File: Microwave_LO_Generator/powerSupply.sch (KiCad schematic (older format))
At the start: 33 parts, among them J1 Conn_01x02_Male, J2 Conn_01x02_Male, U2 LT1962-3.3, U3 LT3010, U5 LT1962-5, U6 LT1962-5

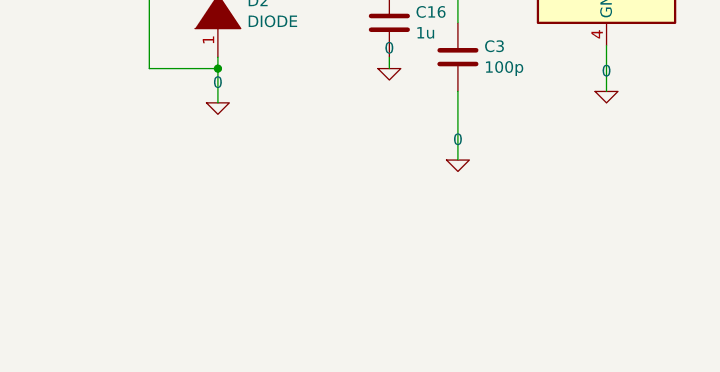
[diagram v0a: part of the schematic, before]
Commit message: ADD GND test probe
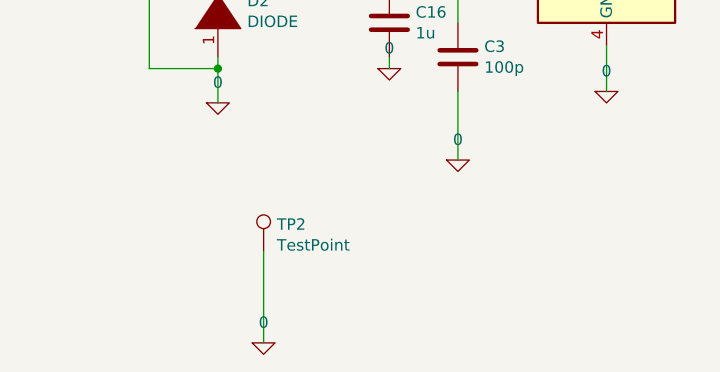
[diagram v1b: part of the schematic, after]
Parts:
- added TP2: TestPoint, TestPoint:TestPoint_Loop_D2.60mm_Drill1.6mm_Beaded, symbol frequencySynthesizer-rescue:TestPoint-frequencySintesizer
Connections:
- net 0: now also TP2.1
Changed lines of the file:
@@
 Wire Wire Line
 	6300 2050 6300 2300
+$Comp
+L pspice:0 #GND0136
+U 1 1 5FCEC166
+P 1750 5400
+F 0 "#GND0136" H 1750 5300 50  0001 C CNN
+F 1 "0" H 1750 5489 50  0000 C CNN
+F 2 "" H 1750 5400 50  0001 C CNN
+F 3 "~" H 1750 5400 50  0001 C CNN
+	1    1750 5400
+	1    0    0    -1
+$EndComp
+$Comp
+L frequencySynthesizer-rescue:TestPoint-frequencySintesizer TP?
+U 1 1 5FCF081C
+P 1750 5000
+AR Path="/5FBD30A7/5FCF081C" Ref="TP?"  Part="1"
+AR Path="/5FBD5B32/5FCF081C" Ref="TP2"  Part="1"
+F 0 "TP2" H 1808 5118 50  0000 L CNN
+F 1 "TestPoint" H 1808 5027 50  0000 L CNN
+F 2 "TestPoint:TestPoint_Loop_D2.60mm_Drill1.6mm_Beaded" H 1950 5000 50  0001 C CNN
+F 3 "https://www.mouser.it/datasheet/2/215/005-5009-741293.pdf" H 1950 5000 50  0001 C CNN
+F 4 "5007" H 1750 5000 50  0001 C CNN "Manufacturer/Part Number"
+F 5 "Mouser 534-5007" H 1750 5000 50  0001 C CNN "Supplier Stock Code"
+	1    1750 5000
+	1    0    0    -1
+$EndComp
+Wire Wire Line
+	1750 5000 1750 5400
 $EndSCHEMATC

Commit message: backup
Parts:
- C16: Manufacturer/Part Number GCM1555C1H101JA16D -> 963-GMK105CC6105MV-F; Supplier Stock Code Mouser 81-GCM1555C1H101JA6D -> GMK105CC6105MV-F
- C17, C19, C23: Manufacturer/Part Number GCM1555C1H101JA16D -> 0402YD475MAT2A; Supplier Stock Code Mouser 81-GCM1555C1H101JA6D -> 581-0402YD475MAT2A
- C21, C24, C31: Supplier Stock Code Mouser 81-GCM1555C1H101JA6D -> 81-GCM1555C1H101JA6D
- C22: Manufacturer/Part Number GCM1555C1H101JA16D -> GMK105CC6105MV-F; Supplier Stock Code Mouser 81-GCM1555C1H101JA6D -> 963-GMK105CC6105MV-F
- C25, C35, C36: Manufacturer/Part Number GCM1555C1H101JA16D -> C1005X5R1A335K050BC; Supplier Stock Code Mouser 81-GCM1555C1H101JA6D -> 810-C1005X5R1A335K0C
- C3, C5: Manufacturer/Part Number GCM1555C1H101JA16D -> 04025C101KAT2A; Supplier Stock Code Mouser 81-GCM1555C1H101JA6D -> 581-04025C101KAT2A
- C32, C33, C34: Manufacturer/Part Number GCM1555C1H101JA16D -> 0402YC103KAT4A; Supplier Stock Code Mouser 81-GCM1555C1H101JA6D -> 581-0402YC103KAT4A
- D2, D3: Manufacturer/Part Number (none) -> LL4002G; Supplier Stock Code (none) -> 821-LL4002G
- D7: Manufacturer/Part Number HSMG-C170 -> AP2012HD; Supplier Stock Code Mouser 630-HSMG-C170 -> 604-AP2012HD
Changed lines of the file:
@@
 F 2 "Capacitor_SMD:C_0402_1005Metric_Pad0.74x0.62mm_HandSolder" H 2338 3850 50  0001 C CNN
 F 3 "~" H 2300 4000 50  0001 C CNN
-F 4 "GCM1555C1H101JA16D" H 2300 4000 50  0001 C CNN "Manufacturer/Part Number"
-F 5 "Mouser 81-GCM1555C1H101JA6D" H 2300 4000 50  0001 C CNN "Supplier Stock Code"
+F 4 "963-GMK105CC6105MV-F" H 2300 4000 50  0001 C CNN "Manufacturer/Part Number"
+F 5 "GMK105CC6105MV-F" H 2300 4000 50  0001 C CNN "Supplier Stock Code"
 	1    2300 4000
 	-1   0    0    1
@@
 F 2 "Diode_SMD:D_MELF" H 1550 3950 50  0001 C CNN
 F 3 "~" H 1550 3950 50  0001 C CNN
+F 4 "LL4002G" V 1550 3950 50  0001 C CNN "Manufacturer/Part Number"
+F 5 "821-LL4002G" V 1550 3950 50  0001 C CNN "Supplier Stock Code"
 	1    1550 3950
 	0    -1   -1   0
@@
 F 2 "Capacitor_SMD:C_0402_1005Metric_Pad0.74x0.62mm_HandSolder" H 4938 3850 50  0001 C CNN
 F 3 "~" H 4900 4000 50  0001 C CNN
-F 4 "GCM1555C1H101JA16D" H 4900 4000 50  0001 C CNN "Manufacturer/Part Number"
-F 5 "Mouser 81-GCM1555C1H101JA6D" H 4900 4000 50  0001 C CNN "Supplier Stock Code"
+F 4 "GMK105CC6105MV-F" H 4900 4000 50  0001 C CNN "Manufacturer/Part Number"
+F 5 "963-GMK105CC6105MV-F" H 4900 4000 50  0001 C CNN "Supplier Stock Code"
 	1    4900 4000
 	-1   0    0    1
@@
 F 2 "Capacitor_SMD:C_0402_1005Metric_Pad0.74x0.62mm_HandSolder" H 7388 1750 50  0001 C CNN
 F 3 "~" H 7350 1900 50  0001 C CNN
-F 4 "GCM1555C1H101JA16D" H 7350 1900 50  0001 C CNN "Manufacturer/Part Number"
-F 5 "Mouser 81-GCM1555C1H101JA6D" H 7350 1900 50  0001 C CNN "Supplier Stock Code"
+F 4 "0402YD475MAT2A" H 7350 1900 50  0001 C CNN "Manufacturer/Part Number"
+F 5 "581-0402YD475MAT2A" H 7350 1900 50  0001 C CNN "Supplier Stock Code"
 	1    7350 1900
 	-1   0    0    1
@@
 F 3 "~" H 7800 2050 50  0001 C CNN
 F 4 "GCM1555C1H101JA16D" H 7800 2050 50  0001 C CNN "Manufacturer/Part Number"
-F 5 "Mouser 81-GCM1555C1H101JA6D" H 7800 2050 50  0001 C CNN "Supplier Stock Code"
+F 5 "81-GCM1555C1H101JA6D" H 7800 2050 50  0001 C CNN "Supplier Stock Code"
 	1    7800 2050
 	-1   0    0    1
@@
 F 2 "Capacitor_SMD:C_0402_1005Metric_Pad0.74x0.62mm_HandSolder" H 9838 1750 50  0001 C CNN
 F 3 "~" H 9800 1900 50  0001 C CNN
-F 4 "GCM1555C1H101JA16D" H 9800 1900 50  0001 C CNN "Manufacturer/Part Number"
-F 5 "Mouser 81-GCM1555C1H101JA6D" H 9800 1900 50  0001 C CNN "Supplier Stock Code"
+F 4 "C1005X5R1A335K050BC" H 9800 1900 50  0001 C CNN "Manufacturer/Part Number"
+F 5 "810-C1005X5R1A335K0C" H 9800 1900 50  0001 C CNN "Supplier Stock Code"
 	1    9800 1900
 	-1   0    0    1
@@
 F 2 "LED_SMD:LED_0805_2012Metric_Pad1.15x1.40mm_HandSolder" H 10250 2300 50  0001 C CNN
 F 3 "https://www.mouser.it/datasheet/2/678/av02-0551en-ds-hsmx-cxxx-05mar2012-1827675.pdf" H 10250 2300 50  0001 C CNN
-F 4 "HSMG-C170" H 10250 2300 50  0001 C CNN "Manufacturer/Part Number"
-F 5 "Mouser 630-HSMG-C170" H 10250 2300 50  0001 C CNN "Supplier Stock Code"
+F 4 "AP2012HD" H 10250 2300 50  0001 C CNN "Manufacturer/Part Number"
+F 5 "604-AP2012HD" H 10250 2300 50  0001 C CNN "Supplier Stock Code"
 	1    10250 2300
 	0    -1   -1   0
@@
 F 2 "Capacitor_SMD:C_0402_1005Metric_Pad0.74x0.62mm_HandSolder" H 9938 3350 50  0001 C CNN
 F 3 "~" H 9900 3500 50  0001 C CNN
-F 4 "GCM1555C1H101JA16D" H 9900 3500 50  0001 C CNN "Manufacturer/Part Number"
-F 5 "Mouser 81-GCM1555C1H101JA6D" H 9900 3500 50  0001 C CNN "Supplier Stock Code"
+F 4 "C1005X5R1A335K050BC" H 9900 3500 50  0001 C CNN "Manufacturer/Part Number"
+F 5 "810-C1005X5R1A335K0C" H 9900 3500 50  0001 C CNN "Supplier Stock Code"
 	1    9900 3500
 	-1   0    0    1
@@
 F 2 "Capacitor_SMD:C_0402_1005Metric_Pad0.74x0.62mm_HandSolder" H 9438 3300 50  0001 C CNN
 F 3 "~" H 9400 3450 50  0001 C CNN
-F 4 "GCM1555C1H101JA16D" H 9400 3450 50  0001 C CNN "Manufacturer/Part Number"
-F 5 "Mouser 81-GCM1555C1H101JA6D" H 9400 3450 50  0001 C CNN "Supplier Stock Code"
+F 4 "0402YC103KAT4A" H 9400 3450 50  0001 C CNN "Manufacturer/Part Number"
+F 5 "581-0402YC103KAT4A" H 9400 3450 50  0001 C CNN "Supplier Stock Code"
 	1    9400 3450
 	-1   0    0    1
@@
 F 2 "Capacitor_SMD:C_0402_1005Metric_Pad0.74x0.62mm_HandSolder" H 9338 1700 50  0001 C CNN
 F 3 "~" H 9300 1850 50  0001 C CNN
-F 4 "GCM1555C1H101JA16D" H 9300 1850 50  0001 C CNN "Manufacturer/Part Number"
-F 5 "Mouser 81-GCM1555C1H101JA6D" H 9300 1850 50  0001 C CNN "Supplier Stock Code"
+F 4 "0402YC103KAT4A" H 9300 1850 50  0001 C CNN "Manufacturer/Part Number"
+F 5 "581-0402YC103KAT4A" H 9300 1850 50  0001 C CNN "Supplier Stock Code"
 	1    9300 1850
 	-1   0    0    1
@@
 F 2 "Capacitor_SMD:C_0402_1005Metric_Pad0.74x0.62mm_HandSolder" H 7438 3350 50  0001 C CNN
 F 3 "~" H 7400 3500 50  0001 C CNN
-F 4 "GCM1555C1H101JA16D" H 7400 3500 50  0001 C CNN "Manufacturer/Part Number"
-F 5 "Mouser 81-GCM1555C1H101JA6D" H 7400 3500 50  0001 C CNN "Supplier Stock Code"
+F 4 "0402YD475MAT2A" H 7400 3500 50  0001 C CNN "Manufacturer/Part Number"
+F 5 "581-0402YD475MAT2A" H 7400 3500 50  0001 C CNN "Supplier Stock Code"
 	1    7400 3500
 	-1   0    0    1
@@
 F 3 "~" H 7850 3650 50  0001 C CNN
 F 4 "GCM1555C1H101JA16D" H 7850 3650 50  0001 C CNN "Manufacturer/Part Number"
-F 5 "Mouser 81-GCM1555C1H101JA6D" H 7850 3650 50  0001 C CNN "Supplier Stock Code"
+F 5 "81-GCM1555C1H101JA6D" H 7850 3650 50  0001 C CNN "Supplier Stock Code"
 	1    7850 3650
 	-1   0    0    1
@@
 F 2 "Capacitor_SMD:C_0402_1005Metric_Pad0.74x0.62mm_HandSolder" H 9938 4650 50  0001 C CNN
 F 3 "~" H 9900 4800 50  0001 C CNN
-F 4 "GCM1555C1H101JA16D" H 9900 4800 50  0001 C CNN "Manufacturer/Part Number"
-F 5 "Mouser 81-GCM1555C1H101JA6D" H 9900 4800 50  0001 C CNN "Supplier Stock Code"
+F 4 "C1005X5R1A335K050BC" H 9900 4800 50  0001 C CNN "Manufacturer/Part Number"
+F 5 "810-C1005X5R1A335K0C" H 9900 4800 50  0001 C CNN "Supplier Stock Code"
 	1    9900 4800
 	-1   0    0    1
@@
 F 2 "Capacitor_SMD:C_0402_1005Metric_Pad0.74x0.62mm_HandSolder" H 9438 4600 50  0001 C CNN
 F 3 "~" H 9400 4750 50  0001 C CNN
-F 4 "GCM1555C1H101JA16D" H 9400 4750 50  0001 C CNN "Manufacturer/Part Number"
-F 5 "Mouser 81-GCM1555C1H101JA6D" H 9400 4750 50  0001 C CNN "Supplier Stock Code"
+F 4 "0402YC103KAT4A" H 9400 4750 50  0001 C CNN "Manufacturer/Part Number"
+F 5 "581-0402YC103KAT4A" H 9400 4750 50  0001 C CNN "Supplier Stock Code"
 	1    9400 4750
 	-1   0    0    1
@@
 F 2 "Capacitor_SMD:C_0402_1005Metric_Pad0.74x0.62mm_HandSolder" H 7438 4650 50  0001 C CNN
 F 3 "~" H 7400 4800 50  0001 C CNN
-F 4 "GCM1555C1H101JA16D" H 7400 4800 50  0001 C CNN "Manufacturer/Part Number"
-F 5 "Mouser 81-GCM1555C1H101JA6D" H 7400 4800 50  0001 C CNN "Supplier Stock Code"
+F 4 "0402YD475MAT2A" H 7400 4800 50  0001 C CNN "Manufacturer/Part Number"
+F 5 "581-0402YD475MAT2A" H 7400 4800 50  0001 C CNN "Supplier Stock Code"
 	1    7400 4800
 	-1   0    0    1
@@
 F 3 "~" H 7850 4950 50  0001 C CNN
 F 4 "GCM1555C1H101JA16D" H 7850 4950 50  0001 C CNN "Manufacturer/Part Number"
-F 5 "Mouser 81-GCM1555C1H101JA6D" H 7850 4950 50  0001 C CNN "Supplier Stock Code"
+F 5 "81-GCM1555C1H101JA6D" H 7850 4950 50  0001 C CNN "Supplier Stock Code"
 	1    7850 4950
 	-1   0    0    1
@@
 F 2 "Capacitor_SMD:C_0402_1005Metric_Pad0.74x0.62mm_HandSolder" H 4438 3750 50  0001 C CNN
 F 3 "~" H 4400 3900 50  0001 C CNN
-F 4 "GCM1555C1H101JA16D" H 4400 3900 50  0001 C CNN "Manufacturer/Part Number"
-F 5 "Mouser 81-GCM1555C1H101JA6D" H 4400 3900 50  0001 C CNN "Supplier Stock Code"
+F 4 "04025C101KAT2A" H 4400 3900 50  0001 C CNN "Manufacturer/Part Number"
+F 5 "581-04025C101KAT2A" H 4400 3900 50  0001 C CNN "Supplier Stock Code"
 	1    4400 3900
 	-1   0    0    1
@@
 F 2 "Capacitor_SMD:C_0402_1005Metric_Pad0.74x0.62mm_HandSolder" H 2638 4000 50  0001 C CNN
 F 3 "~" H 2600 4150 50  0001 C CNN
-F 4 "GCM1555C1H101JA16D" H 2600 4150 50  0001 C CNN "Manufacturer/Part Number"
-F 5 "Mouser 81-GCM1555C1H101JA6D" H 2600 4150 50  0001 C CNN "Supplier Stock Code"
+F 4 "04025C101KAT2A" H 2600 4150 50  0001 C CNN "Manufacturer/Part Number"
+F 5 "581-04025C101KAT2A" H 2600 4150 50  0001 C CNN "Supplier Stock Code"
 	1    2600 4150
 	-1   0    0    1
@@
 F 2 "Diode_SMD:D_MELF" H 6300 1850 50  0001 C CNN
 F 3 "~" H 6300 1850 50  0001 C CNN
+F 4 "LL4002G" V 6300 1850 50  0001 C CNN "Manufacturer/Part Number"
+F 5 "821-LL4002G" V 6300 1850 50  0001 C CNN "Supplier Stock Code"
 	1    6300 1850
 	0    -1   -1   0

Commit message: update bom
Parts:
- D2, D3: Manufacturer/Part Number LL4002G -> SM4004-W; Supplier Stock Code 821-LL4002G -> 583-SM4004
- U2: renamed from U3; Manufacturer/Part Number (none) -> LT3010EMS8E#PBF; Supplier Stock Code (none) -> 584-LT3010EMS8E#PBF
- U3: renamed from U2; Manufacturer/Part Number (none) -> LT1962EMS8-3.3#PBF; Supplier Stock Code (none) -> 584-1962EMS8-3.3PBF
- U4: renamed from U5; Manufacturer/Part Number (none) -> LT1962EMS8-5#PBF; Supplier Stock Code (none) -> 584-LT1962EMS8-5#PBF
- U5: renamed from U6; Manufacturer/Part Number (none) -> LT1962EMS8-5#PBF; Supplier Stock Code (none) -> 584-LT1962EMS8-5#PBF
- renumbered C16 to C14, C3 to C15, C5 to C16, C22 to C17, C23 to C18, C17 to C19, C19 to C20, C24 to C21, C21 to C22, C31 to C23, C32 to C24, C33 to C25, C34 to C26, C25 to C27, C35 to C28, C36 to C29, D7 to D4, J1 to J2, J2 to J3, R8 to R11, R11 to R12, R12 to R13, R13 to R14

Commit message: Update for DRC
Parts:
- U2: footprint Package_SO:MSOP-8-1EP_3x3mm_P0.65mm_EP1.68x1.88mm -> Microwave_LO_Generator:MSOP-8-1EP_3x3mm_P0.65mm_EP1.68x1.88mm
- U3, U4, U5: footprint Package_SO:MSOP-8_3x3mm_P0.65mm -> Microwave_LO_Generator:MSOP-8_3x3mm_P0.65mm
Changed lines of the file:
@@
 F 0 "U4" H 8800 3867 50  0000 C CNN
 F 1 "LT1962-5" H 8800 3776 50  0000 C CNN
-F 2 "Package_SO:MSOP-8_3x3mm_P0.65mm" H 8800 3050 50  0001 C CNN
+F 2 "Microwave_LO_Generator:MSOP-8_3x3mm_P0.65mm" H 8800 3050 50  0001 C CNN
 F 3 "https://www.analog.com/media/en/technical-documentation/data-sheets/1962fb.pdf" H 8800 2850 50  0001 C CNN
 F 4 "LT1962EMS8-5#PBF" H 8800 3400 50  0001 C CNN "Manufacturer/Part Number"
@@
 F 0 "U3" H 8700 2267 50  0000 C CNN
 F 1 "LT1962-3.3" H 8700 2176 50  0000 C CNN
-F 2 "Package_SO:MSOP-8_3x3mm_P0.65mm" H 8700 1450 50  0001 C CNN
+F 2 "Microwave_LO_Generator:MSOP-8_3x3mm_P0.65mm" H 8700 1450 50  0001 C CNN
 F 3 "https://www.analog.com/media/en/technical-documentation/data-sheets/1962fb.pdf" H 8700 1250 50  0001 C CNN
 F 4 "LT1962EMS8-3.3#PBF" H 8700 1800 50  0001 C CNN "Manufacturer/Part Number"
@@
 F 0 "U5" H 8800 5167 50  0000 C CNN
 F 1 "LT1962-5" H 8800 5076 50  0000 C CNN
-F 2 "Package_SO:MSOP-8_3x3mm_P0.65mm" H 8800 4350 50  0001 C CNN
+F 2 "Microwave_LO_Generator:MSOP-8_3x3mm_P0.65mm" H 8800 4350 50  0001 C CNN
 F 3 "https://www.analog.com/media/en/technical-documentation/data-sheets/1962fb.pdf" H 8800 4150 50  0001 C CNN
 F 4 "LT1962EMS8-5#PBF" H 8800 4700 50  0001 C CNN "Manufacturer/Part Number"
@@
 F 0 "U2" H 3250 4167 50  0000 C CNN
 F 1 "LT3010" H 3250 4076 50  0000 C CNN
-F 2 "Package_SO:MSOP-8-1EP_3x3mm_P0.65mm_EP1.68x1.88mm" H 3250 4125 50  0001 C CNN
+F 2 "Microwave_LO_Generator:MSOP-8-1EP_3x3mm_P0.65mm_EP1.68x1.88mm" H 3250 4125 50  0001 C CNN
 F 3 "https://www.analog.com/media/en/technical-documentation/data-sheets/30105fe.pdf" H 3250 3800 50  0001 C CNN
 F 4 "LT3010EMS8E#PBF" H 3250 3800 50  0001 C CNN "Manufacturer/Part Number"
